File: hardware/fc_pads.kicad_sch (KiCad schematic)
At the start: 56 parts, among them J1 5V, J10 5V, J11 5V, J12 5V, J13 5V, J14 5V, J15 5V, J16 5V, J17 5V, J18 5V, J19 5V, J2 5V, J20 5V, J21 5V, J22 5V, J23 5V, J24 5V, J25 5V, J26 5V, J27 5V, J28 5V, J29 5V, J3 5V, J30 5V, J31 5V, J32 5V, J33 5V, J34 5V, J35 5V, J36 5V, J37 5V, J38 5V, J39 5V, J4 5V, J40 5V, J41 5V, J42 5V, J43 5V, J44 5V, J45 5V, J46 5V, J47 5V, J48 5V, J49 5V, J5 5V, J50 5V, J51 5V, J52 5V, J53 5V, J54 5V, J6 5V, J7 5V, J8 5V, J9 5V, P1 SM08B-SRSS-TB(LF)(SN), U8 SM06B-SRSS-TB(LF)(SN)

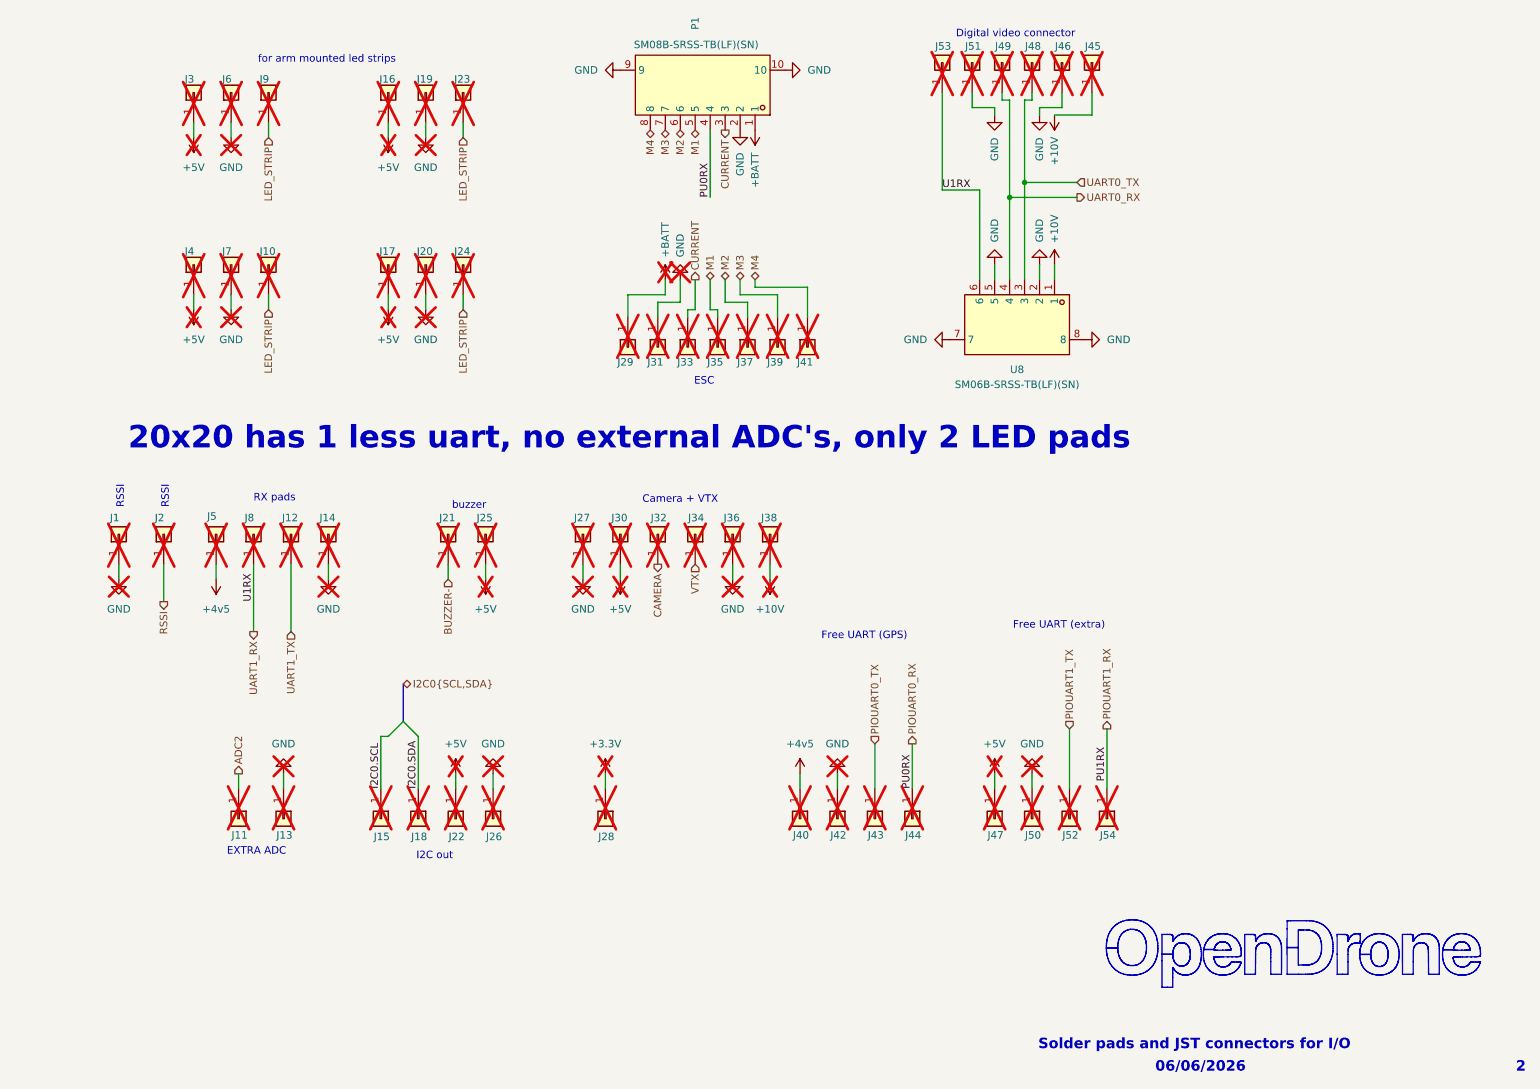
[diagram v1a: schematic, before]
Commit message: Net classes: VBAT, Phase, Power, Gate, USB, RF, Analog with colours and patterns
Replaces the stale 50Ohm /ELRS/* patterns inherited from the template.
Widths and clearances start from the line standard (0.09/0.09, via 0.35/0.20)
and the ESC boards' practice; USB and RF geometry still to be checked against
the chosen JLCPCB 6-layer stackup.
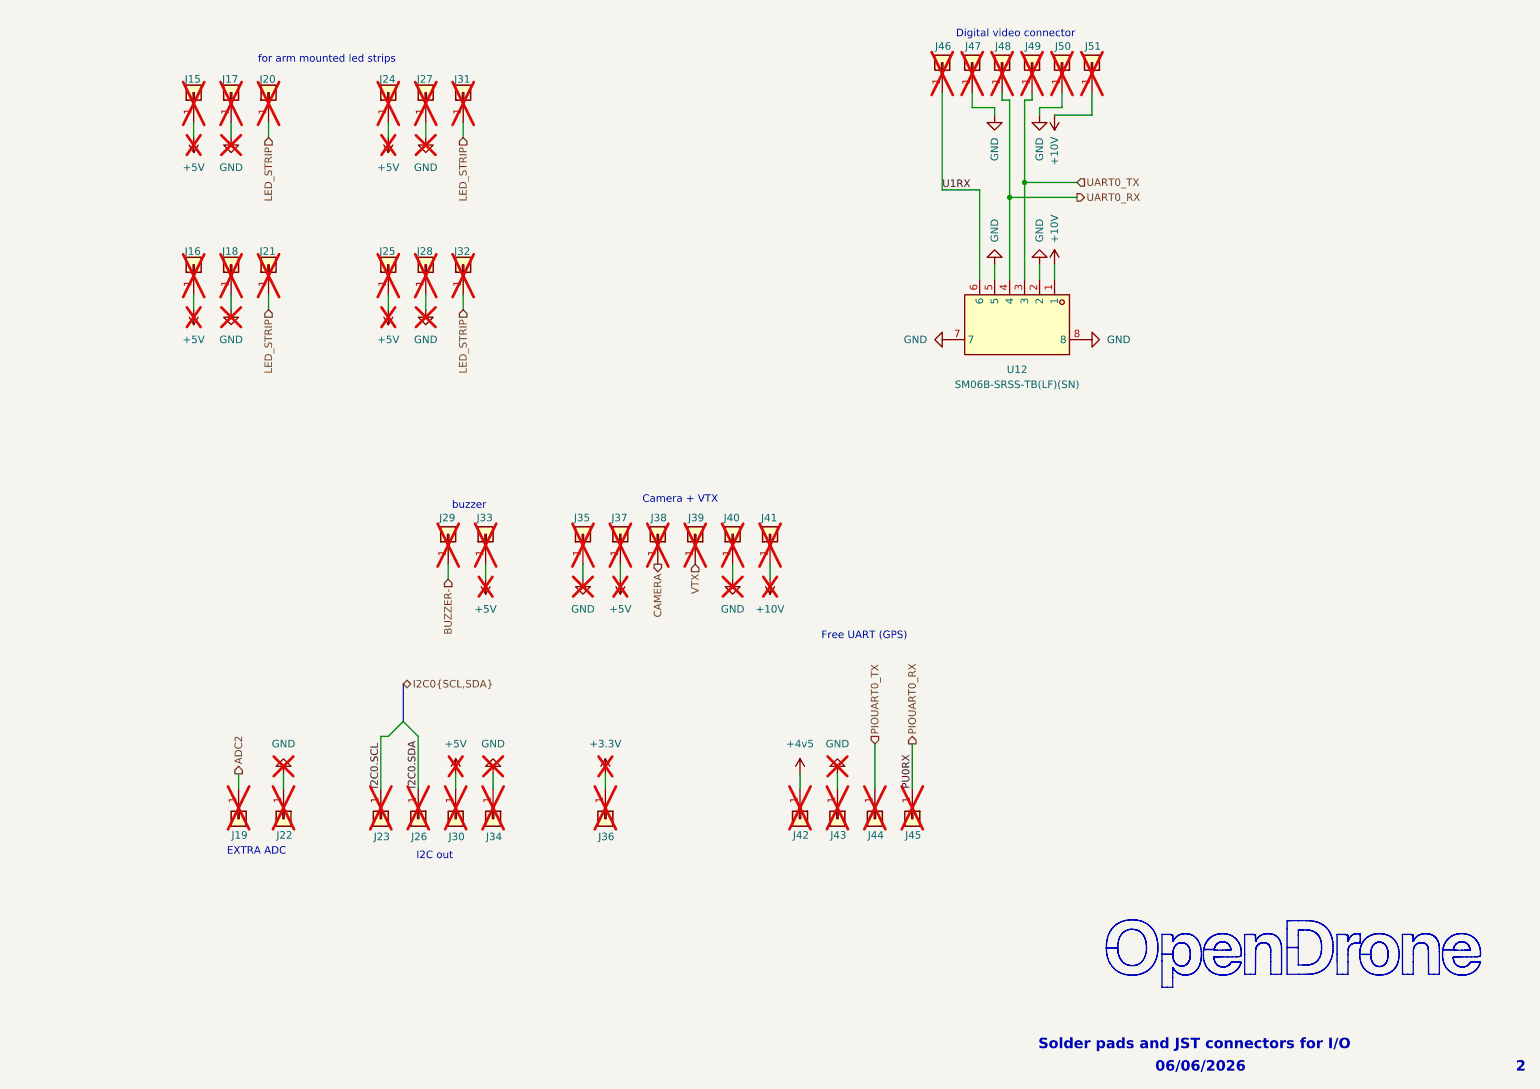
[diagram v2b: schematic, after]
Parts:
- removed J1, J12, J14, J2, J29, J31, J33, J35, J37, J39, J41, J47, J5, J50, J52, J54, J8: 5V, lib:small_pad, symbol Connector_Generic:Conn_01x01
- removed P1: SM08B-SRSS-TB(LF)(SN), lib:CONN-TH_SM08B-SRSS-TB-LF-SN, symbol lib:SM08B-SRSS-TB(LF)(SN)
- renumbered J3 to J15, J4 to J16, J6 to J17, J7 to J18, J11 to J19, J9 to J20, J10 to J21, J13 to J22, J15 to J23, J16 to J24, J17 to J25, J18 to J26, J19 to J27, J20 to J28, J21 to J29, J22 to J30, J23 to J31, J24 to J32, J25 to J33, J26 to J34, J27 to J35, J28 to J36, J30 to J37, J32 to J38, J34 to J39, J36 to J40, J38 to J41, J40 to J42, J42 to J43, J43 to J44, J44 to J45, J53 to J46, J51 to J47, J49 to J48, J48 to J49, J46 to J50, J45 to J51, U8 to U12
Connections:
- net UART1_RX renamed U1RX
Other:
- note removed: "20x20 has 1 less uart, no external ADC's, only 2 LED pads"
- note removed: "ESC"
- note removed: "Free UART (extra)"
- note removed: "RSSI"
- note removed: "RX pads"

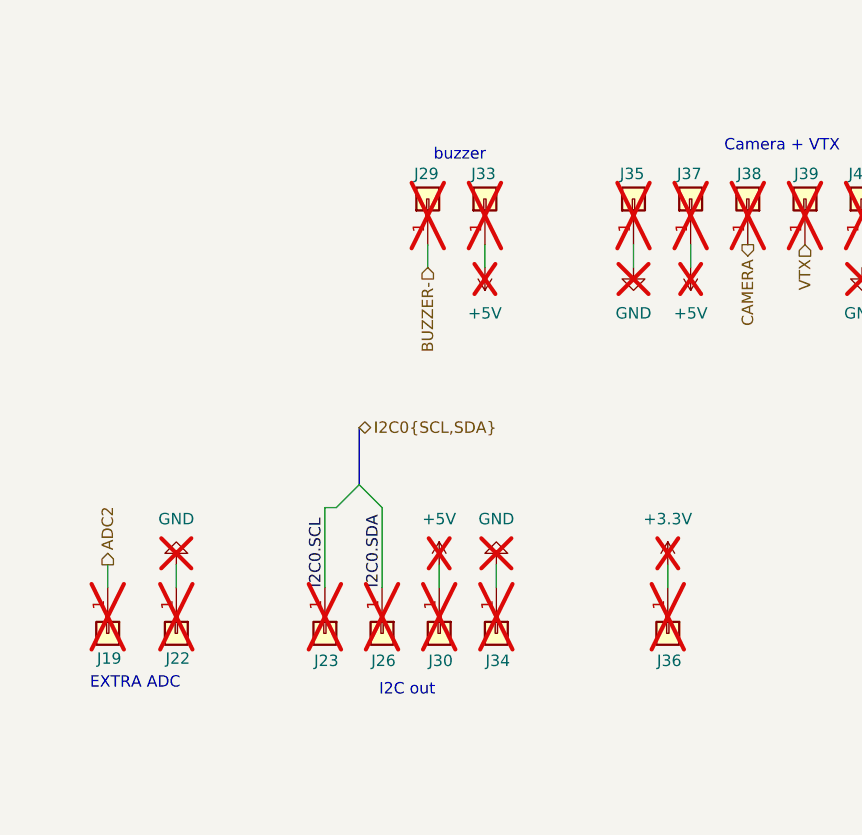
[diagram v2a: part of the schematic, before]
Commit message: OpenAIO: Core outline from User.2 to Edge.Cuts, J90/J91 re-placed with nets, Core rule area, derived boards refreshed
tools/core_outline.py moves the closed User.2 contour of the Core island to
Edge.Cuts. J90 sits in the free area of the Base top (78.9, 62.0), J91 inside
the Core outline (114.1, 53.55) on B.Cu; lga_place.py now assigns pad nets
from the pin table. Rule area Core redrawn from the new outline; split re-run,
J90 carries the new Core STEP and 23.1 x 20.2 mm shadow.
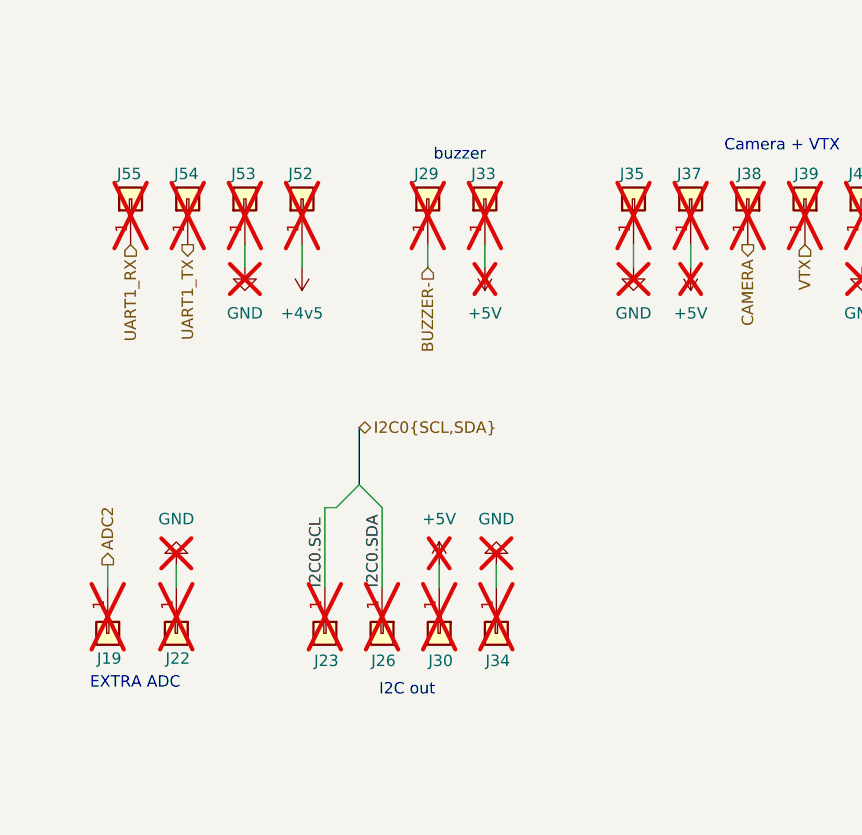
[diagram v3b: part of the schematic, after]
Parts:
- removed J36: 5V, lib:small_pad, symbol Connector_Generic:Conn_01x01
- added J52, J53, J54, J55: 5V, lib:small_pad, symbol Connector_Generic:Conn_01x01
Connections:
- net +4v5: now also J52.1 (Pin_1)
- net GND: now also J53.1 (Pin_1)
- new net UART1_RX: J55.1 (Pin_1)
- new net UART1_TX: J54.1 (Pin_1)
